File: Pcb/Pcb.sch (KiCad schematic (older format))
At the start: 123 parts, among them J1 TRRS, Q1 2N7002, SW1 SW_Push, SW10 SW_Push, SW11 SW_Push, SW12 SW_Push, SW13 SW_Push, SW14 SW_Push, SW15 SW_Push, SW16 SW_Push, SW17 SW_Push, SW18 SW_Push, SW19 SW_Push, SW2 SW2, SW20 SW_Push, SW21 SW_Push, SW22 SW_Push, SW23 SW_Push, SW24 SW_Push, SW25 SW_Push, SW26 SW_Push, SW27 SW_Push, SW28 SW_Push, SW29 SW_Push, SW3 SW_Push, SW4 SW_Push, SW5 SW_Push, SW6 SW_Push, SW7 SW_Push, SW8 SW_Push, SW9 SW_Push, U1 ProMicro

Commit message: Updated footprints
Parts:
- SW1, SW10, SW11, SW12, SW13, SW14, SW15, SW16, SW17, SW18, SW19, SW2, SW20, SW21, SW22, SW23, SW24, SW25, SW26, SW27, SW28, SW3, SW4, SW5, SW6, SW7, SW8, SW9: footprint Used_Footprints:MX_Two_Side -> 1symblos:cherry
- SW29: footprint Used_Footprints:MX_Two_Side -> Used_Footprints:Reset_Switch
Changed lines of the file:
@@
 F 0 "SW1" H 3745 1083 50  0000 C CNN
 F 1 "SW_Push" H 3745 1084 50  0001 C CNN
-F 2 "Used_Footprints:MX_Two_Side" H 3745 1090 50  0001 C CNN
+F 2 "1symblos:cherry" H 3745 1090 50  0001 C CNN
 F 3 "~" H 3745 1090 50  0001 C CNN
 	1    3745 890
@@
 F 0 "SW2" H 4345 1083 50  0000 C CNN
 F 1 "SW2" H 4345 1084 50  0001 C CNN
-F 2 "Used_Footprints:MX_Two_Side" H 4345 1090 50  0001 C CNN
+F 2 "1symblos:cherry" H 4345 1090 50  0001 C CNN
 F 3 "~" H 4345 1090 50  0001 C CNN
 	1    4345 890
@@
 F 0 "SW3" H 4945 1083 50  0000 C CNN
 F 1 "SW_Push" H 4945 1084 50  0001 C CNN
-F 2 "Used_Footprints:MX_Two_Side" H 4945 1090 50  0001 C CNN
+F 2 "1symblos:cherry" H 4945 1090 50  0001 C CNN
 F 3 "~" H 4945 1090 50  0001 C CNN
 	1    4945 890
@@
 F 0 "SW4" H 5545 1083 50  0000 C CNN
 F 1 "SW_Push" H 5545 1084 50  0001 C CNN
-F 2 "Used_Footprints:MX_Two_Side" H 5545 1090 50  0001 C CNN
+F 2 "1symblos:cherry" H 5545 1090 50  0001 C CNN
 F 3 "~" H 5545 1090 50  0001 C CNN
 	1    5545 890
@@
 F 0 "SW5" H 6145 1083 50  0000 C CNN
 F 1 "SW_Push" H 6145 1084 50  0001 C CNN
-F 2 "Used_Footprints:MX_Two_Side" H 6145 1090 50  0001 C CNN
+F 2 "1symblos:cherry" H 6145 1090 50  0001 C CNN
 F 3 "~" H 6145 1090 50  0001 C CNN
 	1    6145 890
@@
 F 0 "SW6" H 6745 1083 50  0000 C CNN
 F 1 "SW_Push" H 6745 1084 50  0001 C CNN
-F 2 "Used_Footprints:MX_Two_Side" H 6745 1090 50  0001 C CNN
+F 2 "1symblos:cherry" H 6745 1090 50  0001 C CNN
 F 3 "~" H 6745 1090 50  0001 C CNN
 	1    6745 890
@@
 F 0 "SW7" H 3745 1483 50  0000 C CNN
 F 1 "SW_Push" H 3745 1484 50  0001 C CNN
-F 2 "Used_Footprints:MX_Two_Side" H 3745 1490 50  0001 C CNN
+F 2 "1symblos:cherry" H 3745 1490 50  0001 C CNN
 F 3 "~" H 3745 1490 50  0001 C CNN
 	1    3745 1290
@@
 F 0 "SW8" H 4345 1483 50  0000 C CNN
 F 1 "SW_Push" H 4345 1484 50  0001 C CNN
-F 2 "Used_Footprints:MX_Two_Side" H 4345 1490 50  0001 C CNN
+F 2 "1symblos:cherry" H 4345 1490 50  0001 C CNN
 F 3 "~" H 4345 1490 50  0001 C CNN
 	1    4345 1290
@@
 F 0 "SW9" H 4945 1483 50  0000 C CNN
 F 1 "SW_Push" H 4945 1484 50  0001 C CNN
-F 2 "Used_Footprints:MX_Two_Side" H 4945 1490 50  0001 C CNN
+F 2 "1symblos:cherry" H 4945 1490 50  0001 C CNN
 F 3 "~" H 4945 1490 50  0001 C CNN
 	1    4945 1290
@@
 F 0 "SW10" H 5545 1483 50  0000 C CNN
 F 1 "SW_Push" H 5545 1484 50  0001 C CNN
-F 2 "Used_Footprints:MX_Two_Side" H 5545 1490 50  0001 C CNN
+F 2 "1symblos:cherry" H 5545 1490 50  0001 C CNN
 F 3 "~" H 5545 1490 50  0001 C CNN
 	1    5545 1290
@@
 F 0 "SW11" H 6145 1483 50  0000 C CNN
 F 1 "SW_Push" H 6145 1484 50  0001 C CNN
-F 2 "Used_Footprints:MX_Two_Side" H 6145 1490 50  0001 C CNN
+F 2 "1symblos:cherry" H 6145 1490 50  0001 C CNN
 F 3 "~" H 6145 1490 50  0001 C CNN
 	1    6145 1290
@@
 F 0 "SW12" H 6745 1483 50  0000 C CNN
 F 1 "SW_Push" H 6745 1484 50  0001 C CNN
-F 2 "Used_Footprints:MX_Two_Side" H 6745 1490 50  0001 C CNN
+F 2 "1symblos:cherry" H 6745 1490 50  0001 C CNN
 F 3 "~" H 6745 1490 50  0001 C CNN
 	1    6745 1290
@@
 F 0 "SW13" H 3745 1883 50  0000 C CNN
 F 1 "SW_Push" H 3745 1884 50  0001 C CNN
-F 2 "Used_Footprints:MX_Two_Side" H 3745 1890 50  0001 C CNN
+F 2 "1symblos:cherry" H 3745 1890 50  0001 C CNN
 F 3 "~" H 3745 1890 50  0001 C CNN
 	1    3745 1690
@@
 F 0 "SW14" H 4345 1883 50  0000 C CNN
 F 1 "SW_Push" H 4345 1884 50  0001 C CNN
-F 2 "Used_Footprints:MX_Two_Side" H 4345 1890 50  0001 C CNN
+F 2 "1symblos:cherry" H 4345 1890 50  0001 C CNN
 F 3 "~" H 4345 1890 50  0001 C CNN
 	1    4345 1690
@@
 F 0 "SW15" H 4945 1883 50  0000 C CNN
 F 1 "SW_Push" H 4945 1884 50  0001 C CNN
-F 2 "Used_Footprints:MX_Two_Side" H 4945 1890 50  0001 C CNN
+F 2 "1symblos:cherry" H 4945 1890 50  0001 C CNN
 F 3 "~" H 4945 1890 50  0001 C CNN
 	1    4945 1690
@@
 F 0 "SW16" H 5545 1883 50  0000 C CNN
 F 1 "SW_Push" H 5545 1884 50  0001 C CNN
-F 2 "Used_Footprints:MX_Two_Side" H 5545 1890 50  0001 C CNN
+F 2 "1symblos:cherry" H 5545 1890 50  0001 C CNN
 F 3 "~" H 5545 1890 50  0001 C CNN
 	1    5545 1690
@@
 F 0 "SW17" H 6145 1883 50  0000 C CNN
 F 1 "SW_Push" H 6145 1884 50  0001 C CNN
-F 2 "Used_Footprints:MX_Two_Side" H 6145 1890 50  0001 C CNN
+F 2 "1symblos:cherry" H 6145 1890 50  0001 C CNN
 F 3 "~" H 6145 1890 50  0001 C CNN
 	1    6145 1690
@@
 F 0 "SW18" H 6745 1883 50  0000 C CNN
 F 1 "SW_Push" H 6745 1884 50  0001 C CNN
-F 2 "Used_Footprints:MX_Two_Side" H 6745 1890 50  0001 C CNN
+F 2 "1symblos:cherry" H 6745 1890 50  0001 C CNN
 F 3 "~" H 6745 1890 50  0001 C CNN
 	1    6745 1690
@@
 F 0 "SW19" H 3745 2283 50  0000 C CNN
 F 1 "SW_Push" H 3745 2284 50  0001 C CNN
-F 2 "Used_Footprints:MX_Two_Side" H 3745 2290 50  0001 C CNN
+F 2 "1symblos:cherry" H 3745 2290 50  0001 C CNN
 F 3 "~" H 3745 2290 50  0001 C CNN
 	1    3745 2090
@@
 F 0 "SW20" H 4345 2283 50  0000 C CNN
 F 1 "SW_Push" H 4345 2284 50  0001 C CNN
-F 2 "Used_Footprints:MX_Two_Side" H 4345 2290 50  0001 C CNN
+F 2 "1symblos:cherry" H 4345 2290 50  0001 C CNN
 F 3 "~" H 4345 2290 50  0001 C CNN
 	1    4345 2090
@@
 F 0 "SW21" H 4945 2283 50  0000 C CNN
 F 1 "SW_Push" H 4945 2284 50  0001 C CNN
-F 2 "Used_Footprints:MX_Two_Side" H 4945 2290 50  0001 C CNN
+F 2 "1symblos:cherry" H 4945 2290 50  0001 C CNN
 F 3 "~" H 4945 2290 50  0001 C CNN
 	1    4945 2090
@@
 F 0 "SW22" H 5545 2283 50  0000 C CNN
 F 1 "SW_Push" H 5545 2284 50  0001 C CNN
-F 2 "Used_Footprints:MX_Two_Side" H 5545 2290 50  0001 C CNN
+F 2 "1symblos:cherry" H 5545 2290 50  0001 C CNN
 F 3 "~" H 5545 2290 50  0001 C CNN
 	1    5545 2090
@@
 F 0 "SW23" H 6145 2283 50  0000 C CNN
 F 1 "SW_Push" H 6145 2284 50  0001 C CNN
-F 2 "Used_Footprints:MX_Two_Side" H 6145 2290 50  0001 C CNN
+F 2 "1symblos:cherry" H 6145 2290 50  0001 C CNN
 F 3 "~" H 6145 2290 50  0001 C CNN
 	1    6145 2090
@@
 F 0 "SW24" H 6745 2283 50  0000 C CNN
 F 1 "SW_Push" H 6745 2284 50  0001 C CNN
-F 2 "Used_Footprints:MX_Two_Side" H 6745 2290 50  0001 C CNN
+F 2 "1symblos:cherry" H 6745 2290 50  0001 C CNN
 F 3 "~" H 6745 2290 50  0001 C CNN
 	1    6745 2090
@@
 F 0 "SW25" H 3745 2683 50  0000 C CNN
 F 1 "SW_Push" H 3745 2684 50  0001 C CNN
-F 2 "Used_Footprints:MX_Two_Side" H 3745 2690 50  0001 C CNN
+F 2 "1symblos:cherry" H 3745 2690 50  0001 C CNN
 F 3 "~" H 3745 2690 50  0001 C CNN
 	1    3745 2490
@@
 F 0 "SW26" H 5545 2683 50  0000 C CNN
 F 1 "SW_Push" H 5545 2684 50  0001 C CNN
-F 2 "Used_Footprints:MX_Two_Side" H 5545 2690 50  0001 C CNN
+F 2 "1symblos:cherry" H 5545 2690 50  0001 C CNN
 F 3 "~" H 5545 2690 50  0001 C CNN
 	1    5545 2490
@@
 F 0 "SW27" H 6145 2683 50  0000 C CNN
 F 1 "SW_Push" H 6145 2684 50  0001 C CNN
-F 2 "Used_Footprints:MX_Two_Side" H 6145 2690 50  0001 C CNN
+F 2 "1symblos:cherry" H 6145 2690 50  0001 C CNN
 F 3 "~" H 6145 2690 50  0001 C CNN
 	1    6145 2490
@@
 F 0 "SW28" H 6745 2683 50  0000 C CNN
 F 1 "SW_Push" H 6745 2684 50  0001 C CNN
-F 2 "Used_Footprints:MX_Two_Side" H 6745 2690 50  0001 C CNN
+F 2 "1symblos:cherry" H 6745 2690 50  0001 C CNN
 F 3 "~" H 6745 2690 50  0001 C CNN
 	1    6745 2490
@@
 F 0 "SW29" H 2625 3395 50  0000 C CNN
 F 1 "SW_Push" H 2625 3304 50  0000 C CNN
-F 2 "Used_Footprints:MX_Two_Side" H 2625 3310 50  0001 C CNN
+F 2 "Used_Footprints:Reset_Switch" H 2625 3310 50  0001 C CNN
 F 3 "~" H 2625 3310 50  0001 C CNN
 	1    2625 3110

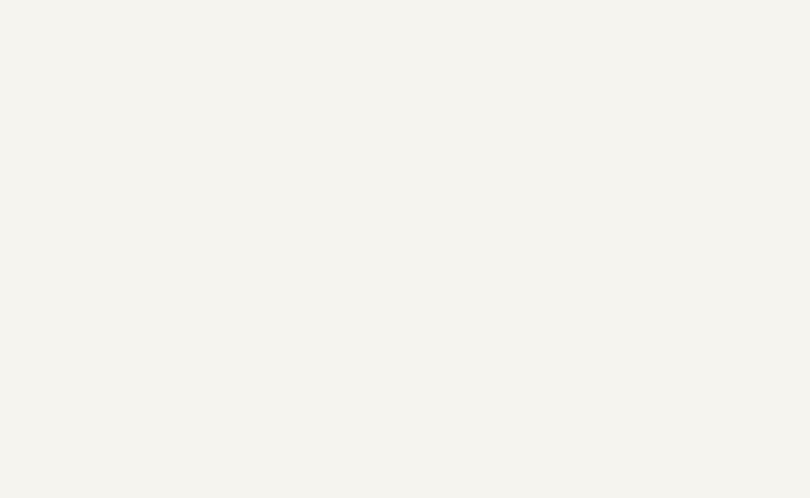
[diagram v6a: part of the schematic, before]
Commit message: Added hole's
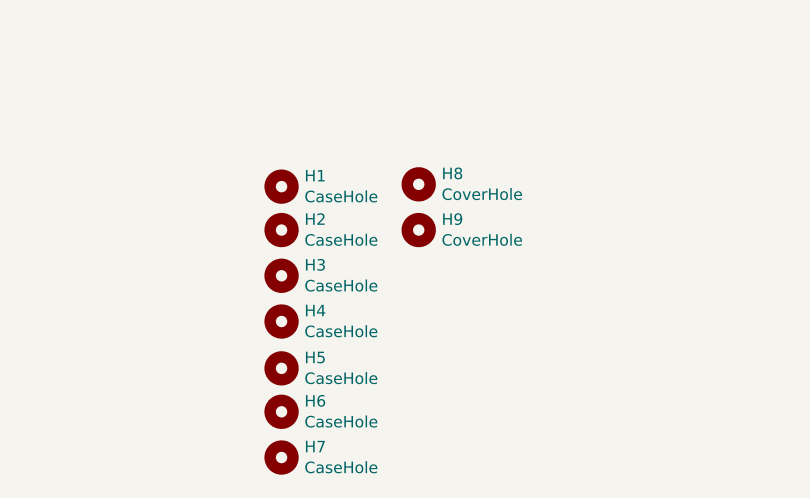
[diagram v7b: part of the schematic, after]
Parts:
- added H1, H2, H3, H4, H5, H6, H7: CaseHole, symbol Mechanical:MountingHole
- added H8, H9: CoverHole, symbol Mechanical:MountingHole
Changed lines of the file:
@@
 Text GLabel 1705 3115 2    50   Input ~ 0
 SCL
+$Comp
+L Mechanical:MountingHole H1
+U 1 1 5DC03D38
+P 7515 4110
+F 0 "H1" H 7615 4156 50  0000 L CNN
+F 1 "CaseHole" H 7615 4065 50  0000 L CNN
+F 2 "" H 7515 4110 50  0001 C CNN
+F 3 "~" H 7515 4110 50  0001 C CNN
+	1    7515 4110
+	1    0    0    -1
+$EndComp
+$Comp
+L Mechanical:MountingHole H2
+U 1 1 5DC0512E
+P 7515 4300
+F 0 "H2" H 7615 4346 50  0000 L CNN
+F 1 "CaseHole" H 7615 4255 50  0000 L CNN
+F 2 "" H 7515 4300 50  0001 C CNN
+F 3 "~" H 7515 4300 50  0001 C CNN
+	1    7515 4300
+	1    0    0    -1
+$EndComp
+$Comp
+L Mechanical:MountingHole H3
+U 1 1 5DC0F92C
+P 7515 4500
+F 0 "H3" H 7615 4546 50  0000 L CNN
+F 1 "CaseHole" H 7615 4455 50  0000 L CNN
+F 2 "" H 7515 4500 50  0001 C CNN
+F 3 "~" H 7515 4500 50  0001 C CNN
+	1    7515 4500
+	1    0    0    -1
+$EndComp
+$Comp
+L Mechanical:MountingHole H4
+U 1 1 5DC14B86
+P 7515 4700
+F 0 "H4" H 7615 4746 50  0000 L CNN
+F 1 "CaseHole" H 7615 4655 50  0000 L CNN
+F 2 "" H 7515 4700 50  0001 C CNN
+F 3 "~" H 7515 4700 50  0001 C CNN
+	1    7515 4700
+	1    0    0    -1
+$EndComp
+$Comp
+L Mechanical:MountingHole H5
+U 1 1 5DC1BC70
+P 7515 4905
+F 0 "H5" H 7615 4951 50  0000 L CNN
+F 1 "CaseHole" H 7615 4860 50  0000 L CNN
+F 2 "" H 7515 4905 50  0001 C CNN
+F 3 "~" H 7515 4905 50  0001 C CNN
+	1    7515 4905
+	1    0    0    -1
+$EndComp
+$Comp
+L Mechanical:MountingHole H6
+U 1 1 5DC1BC76
+P 7515 5095
+F 0 "H6" H 7615 5141 50  0000 L CNN
+F 1 "CaseHole" H 7615 5050 50  0000 L CNN
+F 2 "" H 7515 5095 50  0001 C CNN
+F 3 "~" H 7515 5095 50  0001 C CNN
+	1    7515 5095
+	1    0    0    -1
+$EndComp
+$Comp
+L Mechanical:MountingHole H7
+U 1 1 5DC1BC7C
+P 7515 5295
+F 0 "H7" H 7615 5341 50  0000 L CNN
+F 1 "CaseHole" H 7615 5250 50  0000 L CNN
+F 2 "" H 7515 5295 50  0001 C CNN
+F 3 "~" H 7515 5295 50  0001 C CNN
+	1    7515 5295
+	1    0    0    -1
+$EndComp
+$Comp
+L Mechanical:MountingHole H8
+U 1 1 5DC2660A
+P 8115 4100
+F 0 "H8" H 8215 4146 50  0000 L CNN
+F 1 "CoverHole" H 8215 4055 50  0000 L CNN
+F 2 "" H 8115 4100 50  0001 C CNN
+F 3 "~" H 8115 4100 50  0001 C CNN
+	1    8115 4100
+	1    0    0    -1
+$EndComp
+$Comp
+L Mechanical:MountingHole H9
+U 1 1 5DC26610
+P 8115 4300
+F 0 "H9" H 8215 4346 50  0000 L CNN
+F 1 "CoverHole" H 8215 4255 50  0000 L CNN
+F 2 "" H 8115 4300 50  0001 C CNN
+F 3 "~" H 8115 4300 50  0001 C CNN
+	1    8115 4300
+	1    0    0    -1
+$EndComp
 $EndSCHEMATC

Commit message: Placed hole in correct position
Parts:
- H1, H2, H3, H4, H5, H6, H7: footprint (none) -> Used_Footprints:MountHole
- H8, H9: footprint (none) -> Used_Footprints:CoverHole
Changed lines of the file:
@@
 F 0 "H1" H 7615 4156 50  0000 L CNN
 F 1 "CaseHole" H 7615 4065 50  0000 L CNN
-F 2 "" H 7515 4110 50  0001 C CNN
+F 2 "Used_Footprints:MountHole" H 7515 4110 50  0001 C CNN
 F 3 "~" H 7515 4110 50  0001 C CNN
 	1    7515 4110
@@
 F 0 "H2" H 7615 4346 50  0000 L CNN
 F 1 "CaseHole" H 7615 4255 50  0000 L CNN
-F 2 "" H 7515 4300 50  0001 C CNN
+F 2 "Used_Footprints:MountHole" H 7515 4300 50  0001 C CNN
 F 3 "~" H 7515 4300 50  0001 C CNN
 	1    7515 4300
@@
 F 0 "H3" H 7615 4546 50  0000 L CNN
 F 1 "CaseHole" H 7615 4455 50  0000 L CNN
-F 2 "" H 7515 4500 50  0001 C CNN
+F 2 "Used_Footprints:MountHole" H 7515 4500 50  0001 C CNN
 F 3 "~" H 7515 4500 50  0001 C CNN
 	1    7515 4500
@@
 F 0 "H4" H 7615 4746 50  0000 L CNN
 F 1 "CaseHole" H 7615 4655 50  0000 L CNN
-F 2 "" H 7515 4700 50  0001 C CNN
+F 2 "Used_Footprints:MountHole" H 7515 4700 50  0001 C CNN
 F 3 "~" H 7515 4700 50  0001 C CNN
 	1    7515 4700
@@
 F 0 "H5" H 7615 4951 50  0000 L CNN
 F 1 "CaseHole" H 7615 4860 50  0000 L CNN
-F 2 "" H 7515 4905 50  0001 C CNN
+F 2 "Used_Footprints:MountHole" H 7515 4905 50  0001 C CNN
 F 3 "~" H 7515 4905 50  0001 C CNN
 	1    7515 4905
@@
 F 0 "H6" H 7615 5141 50  0000 L CNN
 F 1 "CaseHole" H 7615 5050 50  0000 L CNN
-F 2 "" H 7515 5095 50  0001 C CNN
+F 2 "Used_Footprints:MountHole" H 7515 5095 50  0001 C CNN
 F 3 "~" H 7515 5095 50  0001 C CNN
 	1    7515 5095
@@
 F 0 "H7" H 7615 5341 50  0000 L CNN
 F 1 "CaseHole" H 7615 5250 50  0000 L CNN
-F 2 "" H 7515 5295 50  0001 C CNN
+F 2 "Used_Footprints:MountHole" H 7515 5295 50  0001 C CNN
 F 3 "~" H 7515 5295 50  0001 C CNN
 	1    7515 5295
@@
 F 0 "H8" H 8215 4146 50  0000 L CNN
 F 1 "CoverHole" H 8215 4055 50  0000 L CNN
-F 2 "" H 8115 4100 50  0001 C CNN
+F 2 "Used_Footprints:CoverHole" H 8115 4100 50  0001 C CNN
 F 3 "~" H 8115 4100 50  0001 C CNN
 	1    8115 4100
@@
 F 0 "H9" H 8215 4346 50  0000 L CNN
 F 1 "CoverHole" H 8215 4255 50  0000 L CNN
-F 2 "" H 8115 4300 50  0001 C CNN
+F 2 "Used_Footprints:CoverHole" H 8115 4300 50  0001 C CNN
 F 3 "~" H 8115 4300 50  0001 C CNN
 	1    8115 4300
